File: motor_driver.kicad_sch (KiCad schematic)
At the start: 8 parts, among them J5 Conn_01x06, J6 Conn_01x06, U11 TB6612FNG

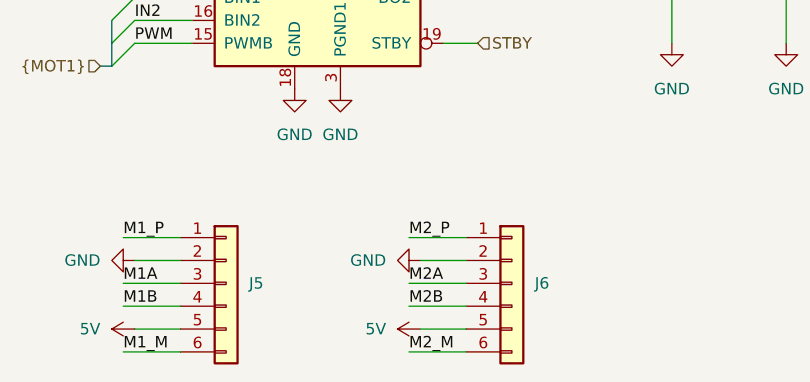
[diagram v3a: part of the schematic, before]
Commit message: Add expansion pin headers
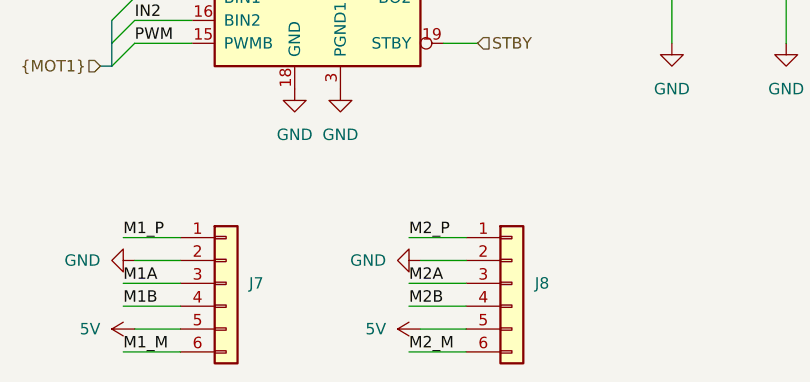
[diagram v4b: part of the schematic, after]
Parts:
- renumbered J5 to J7, J6 to J8
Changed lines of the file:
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@@
 		(dnp no)
 		(fields_autoplaced yes)
-		(property "Reference" "#PWR0140"
+		(property "Reference" "#PWR0154"
 			(at 212.09 78.74 0)
 			(effects
@@
 			(project "Tumbler2_Redesign"
 				(path "/f3fd8d79-9d35-4c04-811e-2697a2740958/f393b342-ddad-47d4-8b4e-f21b64e15add"
-					(reference "#PWR0140")
+					(reference "#PWR0154")
 					(unit 1)
 				)
@@
 		(dnp no)
 		(fields_autoplaced yes)
-		(property "Reference" "#PWR0149"
+		(property "Reference" "#PWR0163"
 			(at 152.4 119.38 0)
 			(effects
@@
 			(project "Tumbler2_Redesign"
 				(path "/f3fd8d79-9d35-4c04-811e-2697a2740958/f393b342-ddad-47d4-8b4e-f21b64e15add"
-					(reference "#PWR0149")
+					(reference "#PWR0163")
 					(unit 1)
 				)
@@
 		(dnp no)
 		(fields_autoplaced yes)
-		(property "Reference" "#PWR0137"
+		(property "Reference" "#PWR0151"
 			(at 149.86 78.74 0)
 			(effects
@@
 			(project "Tumbler2_Redesign"
 				(path "/f3fd8d79-9d35-4c04-811e-2697a2740958/f393b342-ddad-47d4-8b4e-f21b64e15add"
-					(reference "#PWR0137")
+					(reference "#PWR0151")
 					(unit 1)
 				)
@@
 		(dnp no)
 		(fields_autoplaced yes)
-		(property "Reference" "#PWR0136"
+		(property "Reference" "#PWR0150"
 			(at 144.78 78.74 0)
 			(effects
@@
 			(project "Tumbler2_Redesign"
 				(path "/f3fd8d79-9d35-4c04-811e-2697a2740958/f393b342-ddad-47d4-8b4e-f21b64e15add"
-					(reference "#PWR0136")
+					(reference "#PWR0150")
 					(unit 1)
 				)
@@
 		(dnp no)
 		(fields_autoplaced yes)
-		(property "Reference" "#PWR0150"
+		(property "Reference" "#PWR0164"
 			(at 130.81 127 0)
 			(effects
@@
 			(project "Tumbler2_Redesign"
 				(path "/f3fd8d79-9d35-4c04-811e-2697a2740958/f393b342-ddad-47d4-8b4e-f21b64e15add"
-					(reference "#PWR0150")
+					(reference "#PWR0164")
 					(unit 1)
 				)
@@
 		(dnp no)
 		(fields_autoplaced yes)
-		(property "Reference" "#PWR0151"
+		(property "Reference" "#PWR0165"
 			(at 162.56 127 0)
 			(effects
@@
 			(project "Tumbler2_Redesign"
 				(path "/f3fd8d79-9d35-4c04-811e-2697a2740958/f393b342-ddad-47d4-8b4e-f21b64e15add"
-					(reference "#PWR0151")
+					(reference "#PWR0165")
 					(unit 1)
 				)
@@
 		(dnp no)
 		(fields_autoplaced yes)
-		(property "Reference" "#PWR0142"
+		(property "Reference" "#PWR0156"
 			(at 104.14 101.6 0)
 			(effects
@@
 			(project "Tumbler2_Redesign"
 				(path "/f3fd8d79-9d35-4c04-811e-2697a2740958/f393b342-ddad-47d4-8b4e-f21b64e15add"
-					(reference "#PWR0142")
+					(reference "#PWR0156")
 					(unit 1)
 				)
@@
 		(dnp no)
 		(fields_autoplaced yes)
-		(property "Reference" "#PWR0146"
+		(property "Reference" "#PWR0160"
 			(at 144.78 106.68 0)
 			(effects
@@
 			(project "Tumbler2_Redesign"
 				(path "/f3fd8d79-9d35-4c04-811e-2697a2740958/f393b342-ddad-47d4-8b4e-f21b64e15add"
-					(reference "#PWR0146")
+					(reference "#PWR0160")
 					(unit 1)
 				)
@@
 		(dnp no)
 		(fields_autoplaced yes)
-		(property "Reference" "#PWR0148"
+		(property "Reference" "#PWR0162"
 			(at 120.65 119.38 0)
 			(effects
@@
 			(project "Tumbler2_Redesign"
 				(path "/f3fd8d79-9d35-4c04-811e-2697a2740958/f393b342-ddad-47d4-8b4e-f21b64e15add"
-					(reference "#PWR0148")
+					(reference "#PWR0162")
 					(unit 1)
 				)
@@
 		(dnp no)
 		(fields_autoplaced yes)
-		(property "Reference" "#PWR0138"
+		(property "Reference" "#PWR0152"
 			(at 186.69 78.74 0)
 			(effects
@@
 			(project "Tumbler2_Redesign"
 				(path "/f3fd8d79-9d35-4c04-811e-2697a2740958/f393b342-ddad-47d4-8b4e-f21b64e15add"
-					(reference "#PWR0138")
+					(reference "#PWR0152")
 					(unit 1)
 				)
@@
 		(dnp no)
 		(fields_autoplaced yes)
-		(property "Reference" "#PWR0145"
+		(property "Reference" "#PWR0159"
 			(at 212.09 101.6 0)
 			(effects
@@
 			(project "Tumbler2_Redesign"
 				(path "/f3fd8d79-9d35-4c04-811e-2697a2740958/f393b342-ddad-47d4-8b4e-f21b64e15add"
-					(reference "#PWR0145")
+					(reference "#PWR0159")
 					(unit 1)
 				)
@@
 		(dnp no)
 		(fields_autoplaced yes)
-		(property "Reference" "#PWR0144"
+		(property "Reference" "#PWR0158"
 			(at 199.39 101.6 0)
 			(effects
@@
 			(project "Tumbler2_Redesign"
 				(path "/f3fd8d79-9d35-4c04-811e-2697a2740958/f393b342-ddad-47d4-8b4e-f21b64e15add"
-					(reference "#PWR0144")
+					(reference "#PWR0158")
 					(unit 1)
 				)
@@
 		(dnp no)
 		(fields_autoplaced yes)
-		(property "Reference" "#PWR0135"
+		(property "Reference" "#PWR0149"
 			(at 104.14 78.74 0)
 			(effects
@@
 			(project "Tumbler2_Redesign"
 				(path "/f3fd8d79-9d35-4c04-811e-2697a2740958/f393b342-ddad-47d4-8b4e-f21b64e15add"
-					(reference "#PWR0135")
+					(reference "#PWR0149")
 					(unit 1)
 				)
@@
 		(on_board yes)
 		(dnp no)
-		(property "Reference" "J6"
+		(property "Reference" "J8"
 			(at 171.45 121.9199 0)
 			(effects
@@
 			(project "Tumbler2_Redesign"
 				(path "/f3fd8d79-9d35-4c04-811e-2697a2740958/f393b342-ddad-47d4-8b4e-f21b64e15add"
-					(reference "J6")
+					(reference "J8")
 					(unit 1)
 				)
@@
 		(dnp no)
 		(fields_autoplaced yes)
-		(property "Reference" "#PWR0143"
+		(property "Reference" "#PWR0157"
 			(at 186.69 101.6 0)
 			(effects
@@
 			(project "Tumbler2_Redesign"
 				(path "/f3fd8d79-9d35-4c04-811e-2697a2740958/f393b342-ddad-47d4-8b4e-f21b64e15add"
-					(reference "#PWR0143")
+					(reference "#PWR0157")
 					(unit 1)
 				)
@@
 		(on_board yes)
 		(dnp no)
-		(property "Reference" "J5"
+		(property "Reference" "J7"
 			(at 139.7 121.9199 0)
 			(effects
@@
 			(project "Tumbler2_Redesign"
 				(path "/f3fd8d79-9d35-4c04-811e-2697a2740958/f393b342-ddad-47d4-8b4e-f21b64e15add"
-					(reference "J5")
+					(reference "J7")
 					(unit 1)
 				)
@@
 		(dnp no)
 		(fields_autoplaced yes)
-		(property "Reference" "#PWR0141"
+		(property "Reference" "#PWR0155"
 			(at 91.44 101.6 0)
 			(effects
@@
 			(project "Tumbler2_Redesign"
 				(path "/f3fd8d79-9d35-4c04-811e-2697a2740958/f393b342-ddad-47d4-8b4e-f21b64e15add"
-					(reference "#PWR0141")
+					(reference "#PWR0155")
 					(unit 1)
 				)
@@
 		(dnp no)
 		(fields_autoplaced yes)
-		(property "Reference" "#PWR0139"
+		(property "Reference" "#PWR0153"
 			(at 199.39 78.74 0)
 			(effects
@@
 			(project "Tumbler2_Redesign"
 				(path "/f3fd8d79-9d35-4c04-811e-2697a2740958/f393b342-ddad-47d4-8b4e-f21b64e15add"
-					(reference "#PWR0139")
+					(reference "#PWR0153")
 					(unit 1)
 				)
@@
 		(dnp no)
 		(fields_autoplaced yes)
-		(property "Reference" "#PWR0147"
+		(property "Reference" "#PWR0161"
 			(at 149.86 106.68 0)
 			(effects
@@
 			(project "Tumbler2_Redesign"
 				(path "/f3fd8d79-9d35-4c04-811e-2697a2740958/f393b342-ddad-47d4-8b4e-f21b64e15add"
-					(reference "#PWR0147")
+					(reference "#PWR0161")
 					(unit 1)
 				)
@@
 		(dnp no)
 		(fields_autoplaced yes)
-		(property "Reference" "#PWR0134"
+		(property "Reference" "#PWR0148"
 			(at 91.44 78.74 0)
 			(effects
@@
 			(project "Tumbler2_Redesign"
 				(path "/f3fd8d79-9d35-4c04-811e-2697a2740958/f393b342-ddad-47d4-8b4e-f21b64e15add"
-					(reference "#PWR0134")
-					(unit 1)
-				)
+					(reference "#PWR0148")
+					(unit 1)
+				)

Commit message: Combine peripheral modules
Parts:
- removed C39, C42: 10uF, Capacitor_SMD:C_0603_1608Metric_Pad1.08x0.95mm_HandSolder, symbol Device:C
- removed C40, C41: 100nF, Capacitor_SMD:C_0402_1005Metric_Pad0.74x0.62mm_HandSolder, symbol Device:C
- removed C43: 670uF, Capacitor_SMD:C_0805_2012Metric_Pad1.18x1.45mm_HandSolder, symbol Device:C
- removed J7, J8: Conn_01x06, Connector_JST:JST_PH_S6B-PH-SM4-TB_1x06-1MP_P2.00mm_Horizontal, symbol Connector_Generic:Conn_01x06
- removed U11: TB6612FNG, Package_SO:SSOP-24_5.3x8.2mm_P0.65mm, symbol Driver_Motor:TB6612FNG
